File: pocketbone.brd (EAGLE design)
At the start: 55 x 35 mm, 60 parts, among them J1 USD_CONNECTOR, U1 24LC_32AT-I/OT, U2 OSD3358, U3 SN74LVC1G07_DCK_5, Y1 CM200C-32.768KAZF-UT, Y2 445C33D24M00000

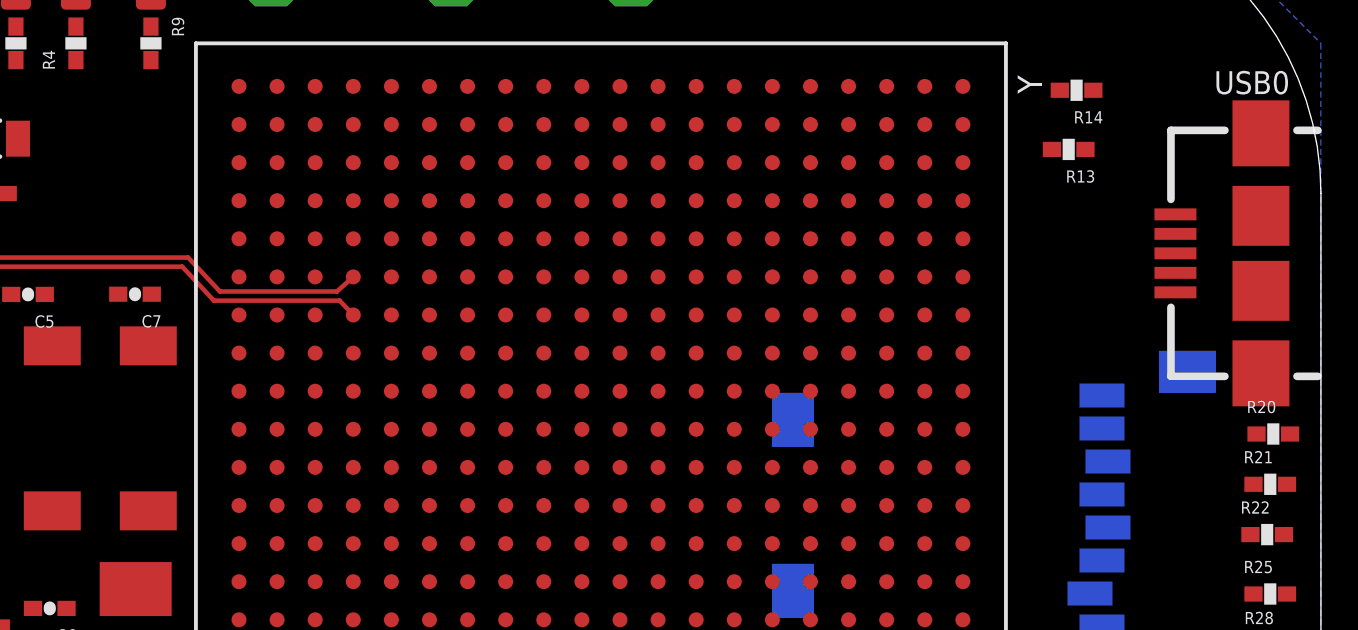
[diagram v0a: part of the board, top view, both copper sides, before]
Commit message: Routed USB0 DP/DN
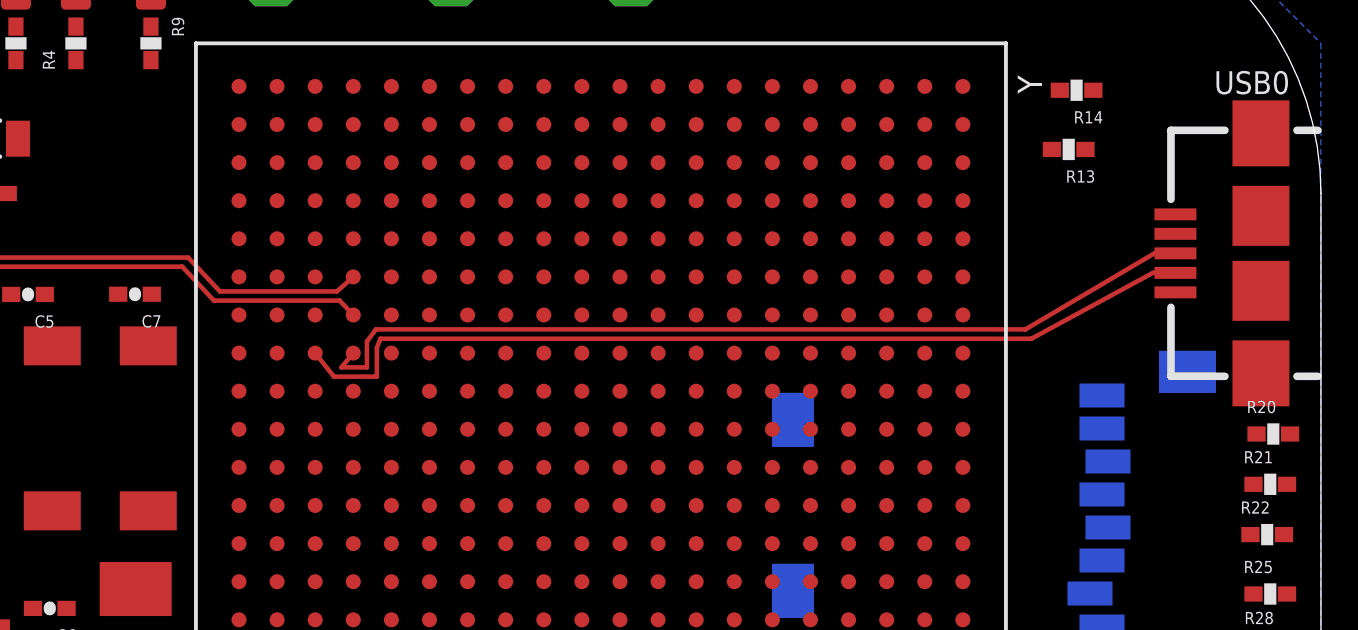
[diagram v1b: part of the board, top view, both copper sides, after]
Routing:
- net USB0_DM: track 0.00 -> 30.8 mm
- net USB0_DP: track 0.00 -> 30.3 mm
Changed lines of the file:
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@@
 <contactref element="U2" pad="N17"/>
 <contactref element="USB0" pad="D+"/>
-<wire x1="22.745" y1="19.675" x2="50.15" y2="23" width="0" layer="19" extent="1-1"/>
+<wire x1="22.745" y1="19.675" x2="22.745" y2="19.705" width="0.1524" layer="1"/>
+<wire x1="23.5" y1="20.465" x2="45.15" y2="20.465" width="0.1524" layer="1"/>
+<wire x1="22.745" y1="19.675" x2="22.745" y2="19.595" width="0.1524" layer="1"/>
+<wire x1="23.2" y1="19.2" x2="23.2" y2="20.065" width="0.1524" layer="1"/>
+<wire x1="23.2" y1="20.065" x2="23.5" y2="20.465" width="0.1524" layer="1"/>
+<wire x1="23.2" y1="19.2" x2="22.35" y2="19.2" width="0.1524" layer="1"/>
+<wire x1="22.35" y1="19.2" x2="22.745" y2="19.675" width="0.1524" layer="1"/>
+<wire x1="45.15" y1="20.465" x2="49.45" y2="23" width="0.1524" layer="1"/>
+<wire x1="49.45" y1="23" x2="50.15" y2="23" width="0.1524" layer="1"/>
 </signal>
 <signal name="USB0_DM" class="2">
 <contactref element="U2" pad="N18"/>
 <contactref element="USB0" pad="D-"/>
-<wire x1="21.475" y1="19.675" x2="50.15" y2="22.35" width="0" layer="19" extent="1-1"/>
+<wire x1="23.65" y1="20.154" x2="45.35" y2="20.154" width="0.1524" layer="1"/>
+<wire x1="45.35" y1="20.154" x2="49.4" y2="22.35" width="0.1524" layer="1"/>
+<wire x1="23.65" y1="20.154" x2="23.53" y2="19.85" width="0.1524" layer="1"/>
+<wire x1="23.53" y1="19.85" x2="23.53" y2="18.89" width="0.1524" layer="1"/>
+<wire x1="23.53" y1="18.89" x2="22.1" y2="18.89" width="0.1524" layer="1"/>
+<wire x1="22.1" y1="18.89" x2="21.475" y2="19.675" width="0.1524" layer="1"/>
+<wire x1="49.4" y1="22.35" x2="50.15" y2="22.35" width="0.1524" layer="1"/>
 </signal>
 <signal name="USB0_ID">
@@
 <wire x1="5.9828" y1="22.86" x2="4.85" y2="23" width="0.1524" layer="1"/>
 <wire x1="5.9828" y1="22.86" x2="17.24" y2="22.86" width="0.1524" layer="1"/>
-<wire x1="17.24" y1="22.86" x2="18.3" y2="21.729" width="0.1524" layer="1"/>
-<wire x1="18.3" y1="21.729" x2="22.2" y2="21.729" width="0.1524" layer="1"/>
-<wire x1="22.2" y1="21.729" x2="22.745" y2="22.215" width="0.1524" layer="1"/>
+<wire x1="17.24" y1="22.86" x2="18.3" y2="21.73" width="0.1524" layer="1"/>
+<wire x1="18.3" y1="21.73" x2="22.2" y2="21.73" width="0.1524" layer="1"/>
+<wire x1="22.2" y1="21.73" x2="22.745" y2="22.215" width="0.1524" layer="1"/>
 </signal>
 <signal name="USB1_DM" class="2">
@@
 <wire x1="4.9564" y1="22.4028" x2="4.85" y2="22.35" width="0.1524" layer="1"/>
 <wire x1="5.9436" y1="22.5552" x2="17.0448" y2="22.5552" width="0.1524" layer="1"/>
-<wire x1="17.0448" y1="22.5552" x2="18.1" y2="21.4238" width="0.1524" layer="1"/>
-<wire x1="18.1" y1="21.4238" x2="22.29" y2="21.4238" width="0.1524" layer="1"/>
-<wire x1="22.29" y1="21.4238" x2="22.745" y2="20.945" width="0.1524" layer="1"/>
+<wire x1="17.0448" y1="22.5552" x2="18.1" y2="21.425" width="0.1524" layer="1"/>
+<wire x1="18.1" y1="21.425" x2="22.29" y2="21.425" width="0.1524" layer="1"/>
+<wire x1="22.29" y1="21.425" x2="22.745" y2="20.945" width="0.1524" layer="1"/>
 </signal>
 <signal name="N$1">

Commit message: New rough placement
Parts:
- moved R12 39.5 mm to (14.2, 24.9), turned to 180 degrees
- moved R11 30.6 mm to (23.2, 31.2), turned to 180 degrees
- moved R23 27.6 mm to (45.9, 33.2)
- moved R28 25.6 mm to (42.9, 33.3)
- moved R26 25.1 mm to (42.6, 30.8), turned to 180 degrees
- moved R25 24.0 mm to (40.2, 31.7)
- moved R19 21.5 mm to (49.9, 31.2)
- moved R22 19.8 mm to (44.9, 31.6)
- moved R16 19.6 mm to (47.3, 30.9)
- moved R18 19.5 mm to (46.3, 25.4)
- moved R17 14.0 mm to (46.3, 23.9)
- moved R21 13.8 mm to (49.5, 28.6)
- moved R20 12.4 mm to (46.3, 27.1)
- moved R27 8.69 mm to (40.3, 33.4)
- moved C3 8.16 mm to (50.8, 12.4)
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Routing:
- net GND: track 0.00 -> 34.7 mm, vias 0 -> 31
- net SYS_5V: track 0.00 -> 32.7 mm
- net N$27: track 0.00 -> 12.0 mm
- net N$31: track 0.00 -> 12.0 mm
- net N$33: track 0.00 -> 7.22 mm
- net N$32: track 0.00 -> 6.40 mm
- net N$26: track 0.00 -> 6.26 mm
- net N$129: track 0.00 -> 4.83 mm
- net 3.3V: track 0.00 -> 1.28 mm

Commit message: Hack layout
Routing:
- net GND: track 34.7 -> 135.1 mm, vias 31 -> 32
- net 3.3V: track 1.28 -> 83.6 mm, vias 0 -> 6
- net NTE: track 0.00 -> 44.9 mm, vias 0 -> 3
- net USB_DC: track 0.00 -> 37.1 mm, vias 0 -> 2
- net N$74: track 0.00 -> 37.0 mm, vias 0 -> 1
- net USB0_ID: track 0.00 -> 35.7 mm, vias 0 -> 4
- net RESET: track 0.00 -> 34.9 mm, vias 0 -> 4
- net I2C0_SCL: track 0.00 -> 34.3 mm, vias 0 -> 4
- net N$77: track 0.00 -> 32.7 mm, vias 0 -> 1
- net VDD_1V8: track 0.00 -> 31.8 mm
- net LDO_PGOOD: track 0.00 -> 31.8 mm, vias 0 -> 4
- net N$5: track 0.00 -> 29.3 mm, vias 0 -> 1
- net SVO6: track 0.00 -> 26.7 mm, vias 0 -> 2
- net N$70: track 0.00 -> 26.3 mm, vias 0 -> 1
- net N$2: track 0.00 -> 26.1 mm, vias 0 -> 3
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
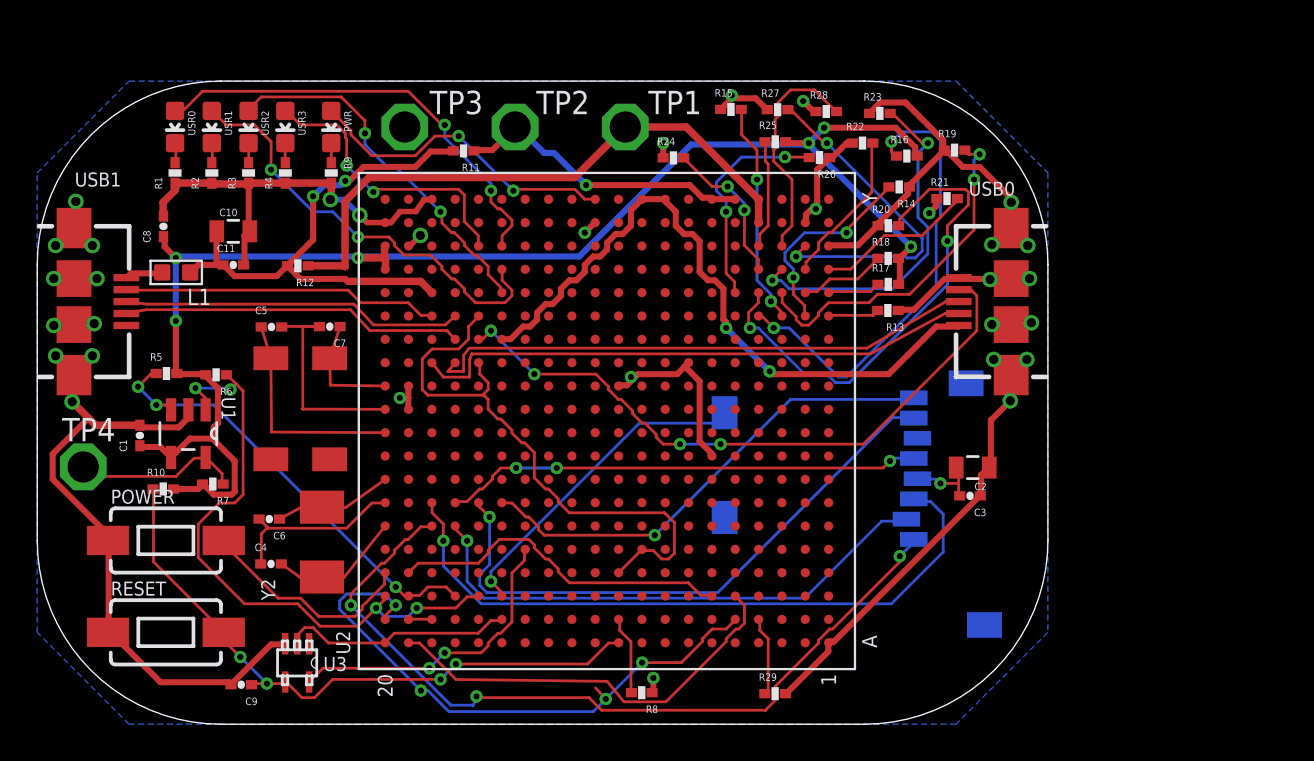
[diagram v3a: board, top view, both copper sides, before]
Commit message: Adjusted resistors for 100% layout
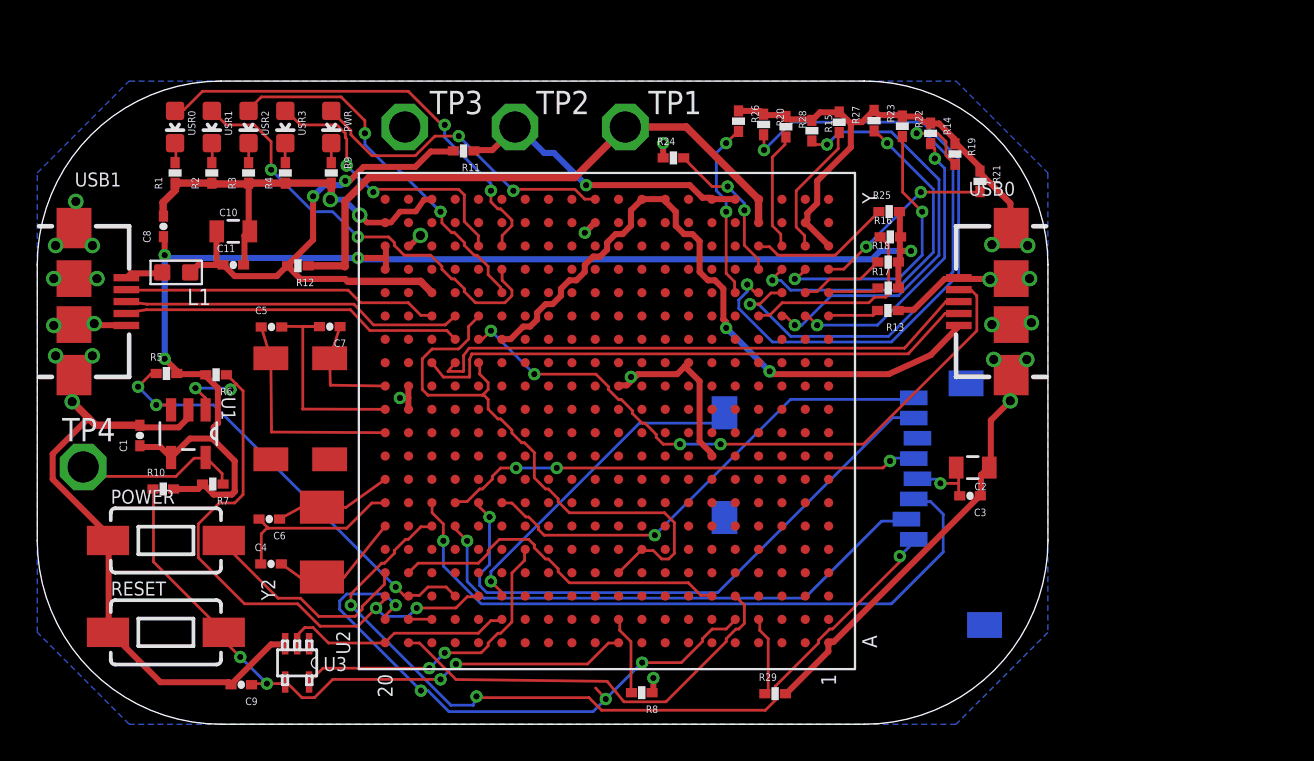
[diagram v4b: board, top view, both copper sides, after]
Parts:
- moved R20 8.74 mm to (39.5, 32.6), turned to 270 degrees
- moved R25 7.27 mm to (46.4, 27.9)
- moved R26 4.83 mm to (38.2, 32.8), turned to 270 degrees
- moved R15 4.55 mm to (42.2, 32.3), turned to 270 degrees
- moved R16 4.49 mm to (46.4, 26.5)
- moved R27 3.42 mm to (43.6, 32.8), turned to 270 degrees
- moved R14 3.38 mm to (48.6, 32.2), turned to 270 degrees
- moved R22 2.35 mm to (47.1, 32.5), turned to 270 degrees
- moved R28 2.35 mm to (40.7, 32.5), turned to 270 degrees
- moved R21 2.02 mm to (51.3, 29.5), turned to 270 degrees
- moved R23 0.50 mm to (45.5, 32.8), turned to 270 degrees
- moved R19 0.21 mm to (49.9, 31.0), turned to 270 degrees
- moved R17 0.20 mm to (46.3, 23.7)
- moved R18 0.20 mm to (46.3, 25.2)
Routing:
- net MDIR_3A: track 25.1 -> 10.9 mm, vias 2 -> 0
- net EQEP_1A: track 18.7 -> 7.35 mm, vias 2 -> 0
- net MDIR_3B: track 12.2 -> 22.8 mm
- net 3.3V: track 83.6 -> 73.6 mm, vias 6 -> 4
- net SVO6: track 26.7 -> 35.8 mm
- net SVO5: track 19.0 -> 27.1 mm
- net UART5_RX: track 8.52 -> 15.2 mm, vias 0 -> 2
- net EQEP_1B: track 12.5 -> 6.47 mm
- net MDIR_4B: track 11.2 -> 15.8 mm
- net GND: track 135.1 -> 137.6 mm, vias 32 -> 27
- net BATT_LED_2: track 12.1 -> 9.71 mm
- net LCD_DATA_14: track 5.96 -> 7.73 mm
- net UART5_TX: track 8.73 -> 9.99 mm, vias 0 -> 2
- net SERVO_EN: track 19.5 -> 18.6 mm

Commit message: Connect microSD to 3.3V
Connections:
- removed net VCC_3V3B: C2.2, C3.2, J1.VCC
- net 3.3V: now also C2.2, C3.2, J1.VCC
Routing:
- net 3.3V: track 73.6 -> 77.6 mm, vias 4 -> 5
- net VCC_3V3B: track 3.97 -> 0.00 mm, vias 1 -> 0
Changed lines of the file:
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@@
 <via x="17.4498" y="25.3746" extent="1-16" drill="0.3302"/>
 <via x="47.5488" y="25.7556" extent="1-16" drill="0.3302"/>
+<contactref element="C3" pad="2"/>
+<contactref element="C2" pad="2"/>
+<contactref element="J1" pad="VCC"/>
+<wire x1="50.1396" y1="13.8684" x2="50.1396" y2="13.1064" width="0.1524" layer="1"/>
+<wire x1="50.1396" y1="13.1064" x2="50.1396" y2="12.4968" width="0.1524" layer="1"/>
+<wire x1="50.0634" y1="13.9446" x2="50.1396" y2="13.8684" width="0.1524" layer="1"/>
+<wire x1="50.1396" y1="12.4968" x2="50.2008" y2="12.4296" width="0.1524" layer="1"/>
+<wire x1="50.0634" y1="13.9446" x2="50.0096" y2="13.9656" width="0.1524" layer="1"/>
+<wire x1="48.9204" y1="13.335" x2="47.9298" y2="13.335" width="0.1524" layer="16"/>
+<wire x1="49.149" y1="13.1064" x2="48.9204" y2="13.335" width="0.1524" layer="16"/>
+<wire x1="50.1396" y1="13.1064" x2="49.149" y2="13.1064" width="0.1524" layer="1"/>
+<wire x1="47.9298" y1="13.335" x2="47.9" y2="13.36" width="0.1524" layer="16"/>
+<via x="49.149" y="13.1064" extent="1-16" drill="0.3302"/>
+<wire x1="46.867" y1="23.737059375" x2="50.0096" y2="13.9656" width="0" layer="19" extent="1-1"/>
 </signal>
 <signal name="VDD_3V3AUX">
@@
 <via x="22.098" y="9.9822" extent="1-16" drill="0.3302"/>
 </signal>
-<signal name="VCC_3V3B">
-<contactref element="C3" pad="2"/>
-<contactref element="C2" pad="2"/>
-<contactref element="J1" pad="VCC"/>
-<wire x1="50.1396" y1="13.8684" x2="50.1396" y2="13.1064" width="0.1524" layer="1"/>
-<wire x1="50.1396" y1="13.1064" x2="50.1396" y2="12.4968" width="0.1524" layer="1"/>
-<wire x1="50.0634" y1="13.9446" x2="50.1396" y2="13.8684" width="0.1524" layer="1"/>
-<wire x1="50.1396" y1="12.4968" x2="50.2008" y2="12.4296" width="0.1524" layer="1"/>
-<wire x1="50.0634" y1="13.9446" x2="50.0096" y2="13.9656" width="0.1524" layer="1"/>
-<wire x1="48.9204" y1="13.335" x2="47.9298" y2="13.335" width="0.1524" layer="16"/>
-<wire x1="49.149" y1="13.1064" x2="48.9204" y2="13.335" width="0.1524" layer="16"/>
-<wire x1="50.1396" y1="13.1064" x2="49.149" y2="13.1064" width="0.1524" layer="1"/>
-<wire x1="47.9298" y1="13.335" x2="47.9" y2="13.36" width="0.1524" layer="16"/>
-<via x="49.149" y="13.1064" extent="1-16" drill="0.3302"/>
-</signal>
 <signal name="NTE">
